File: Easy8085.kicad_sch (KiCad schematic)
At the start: 37 parts, among them J1 5V Power, J2 EXPANSION, J3 FTDI, SW1 RESET, U1 8085, U2 74LS139, U3 74LS573, U4 CY62256, U5 X28256, U6 8251A, U7 74LS90, Y1 6.144M

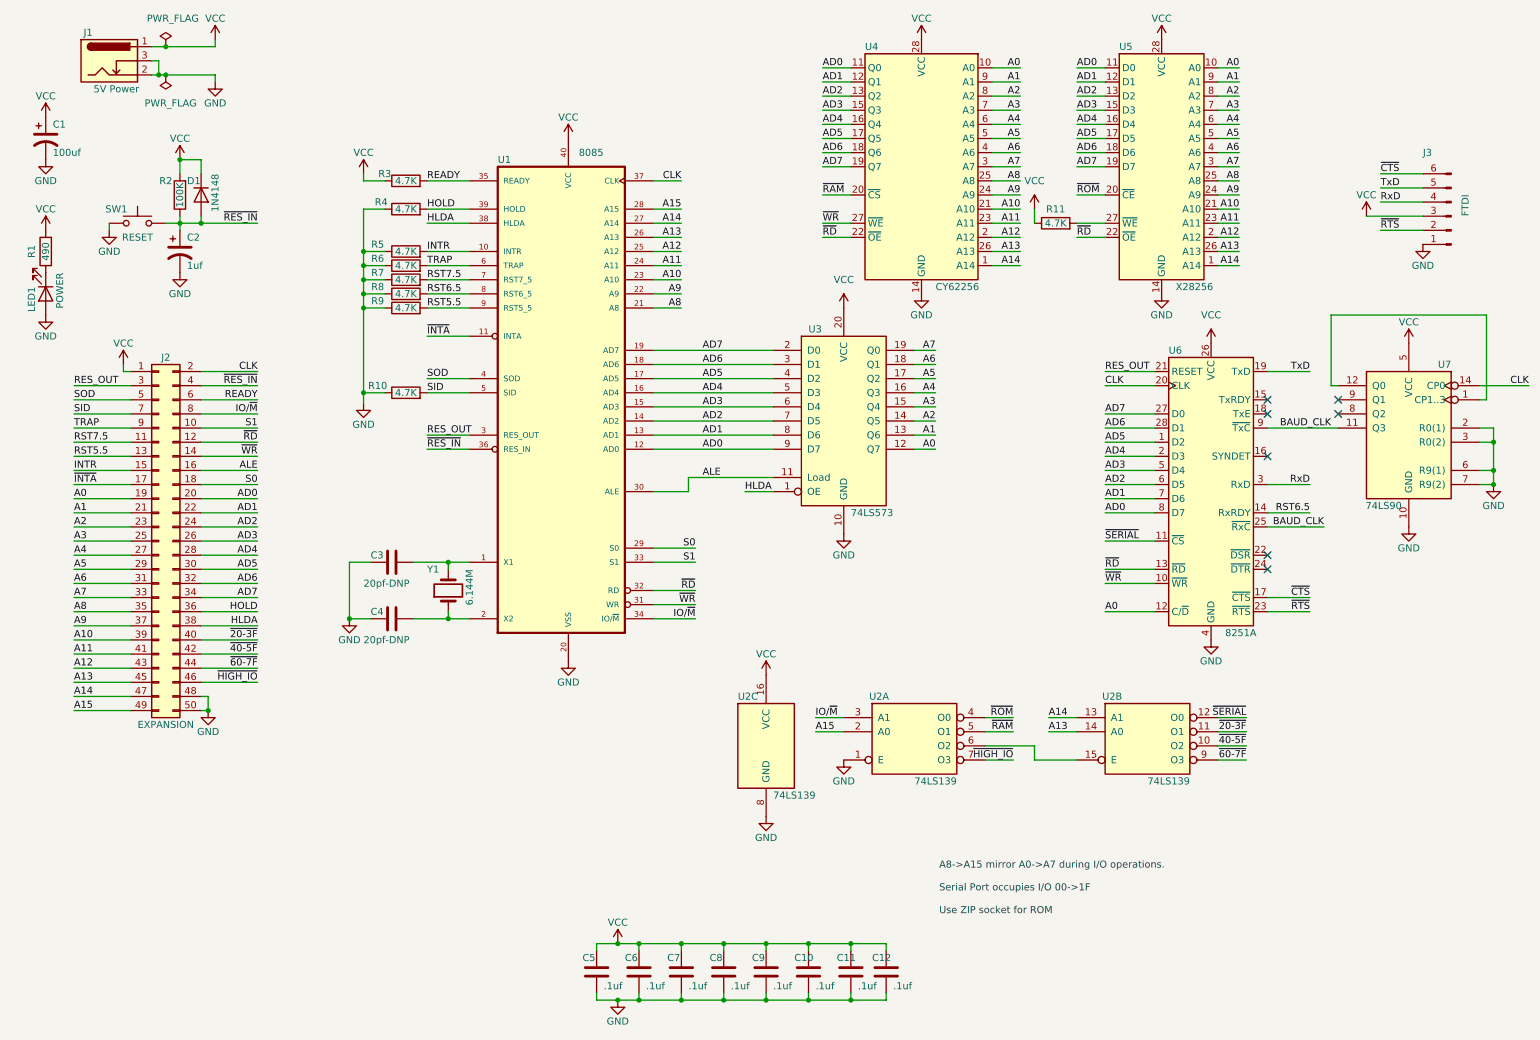
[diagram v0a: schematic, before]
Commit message: re-working PCB and schematic to seperate expansion connector and reduce parts.
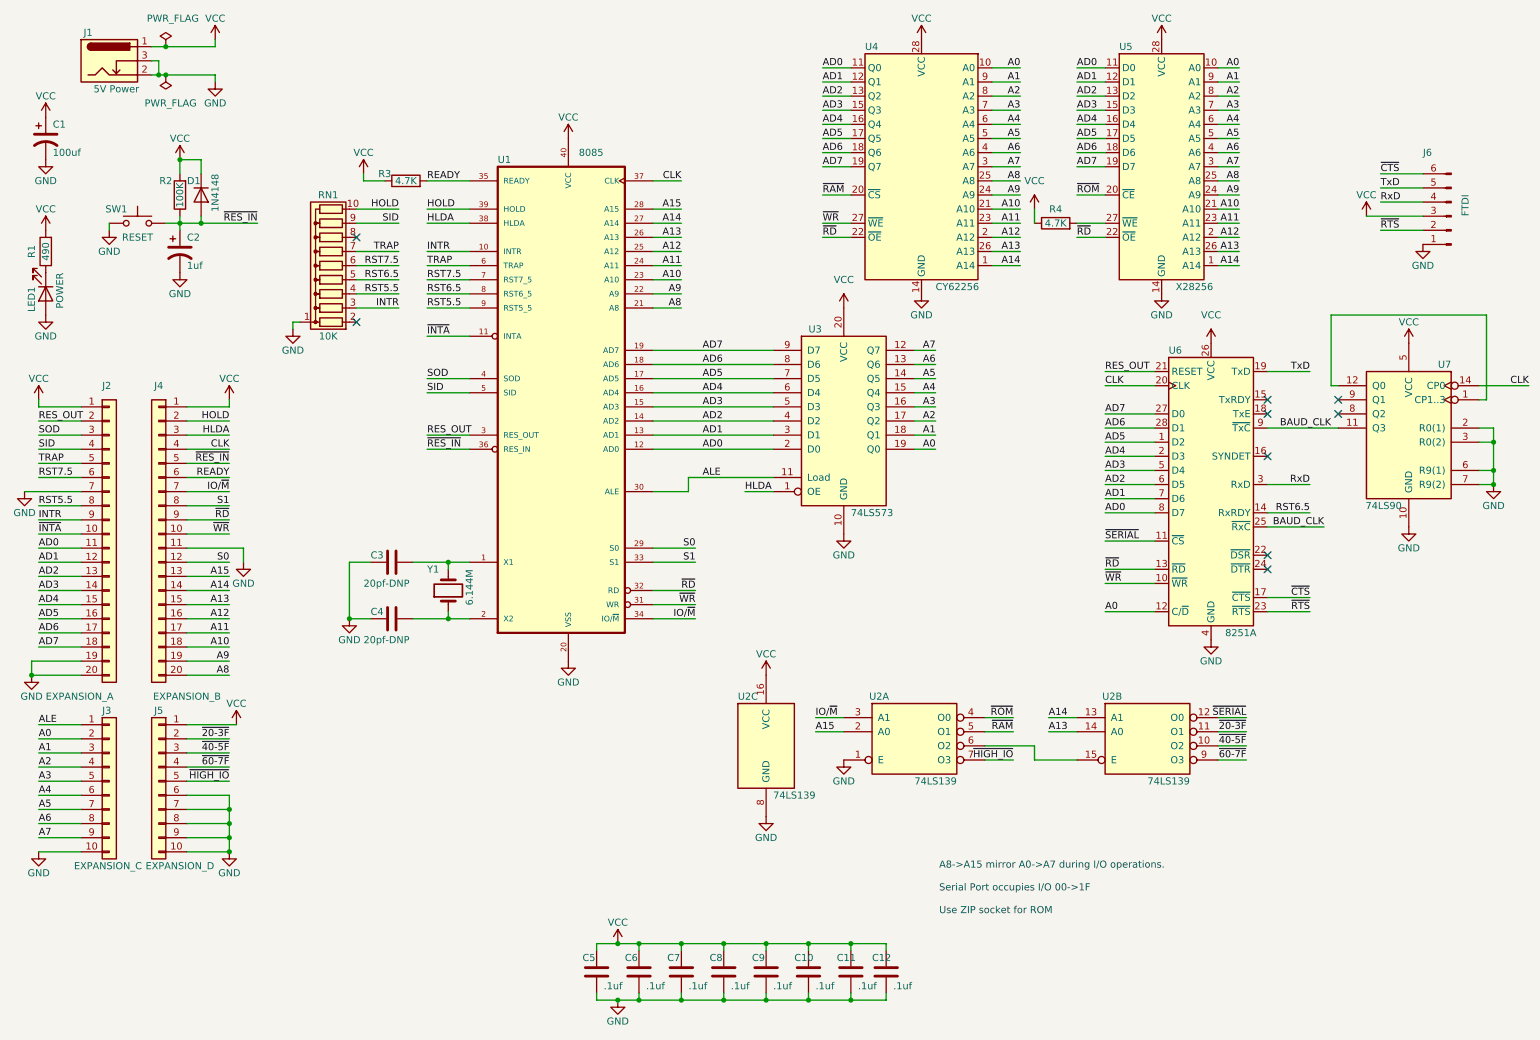
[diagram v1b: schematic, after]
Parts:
- removed J2: EXPANSION, Connector_PinHeader_2.54mm:PinHeader_2x25_P2.54mm_Vertical, symbol Connector_Generic:Conn_02x25_Odd_Even
- removed R10, R4, R5, R6, R7, R8, R9: 4.7K, Resistor_THT:R_Axial_DIN0204_L3.6mm_D1.6mm_P7.62mm_Horizontal, symbol Device:R
- added J2: EXPANSION_A, Connector_PinHeader_2.54mm:PinHeader_1x20_P2.54mm_Vertical, symbol Connector_Generic:Conn_01x20
- added J3: EXPANSION_C, Connector_PinHeader_2.54mm:PinHeader_1x10_P2.54mm_Vertical, symbol Connector_Generic:Conn_01x10
- added J4: EXPANSION_B, Connector_PinHeader_2.54mm:PinHeader_1x20_P2.54mm_Vertical, symbol Connector_Generic:Conn_01x20
- added J5: EXPANSION_D, Connector_PinHeader_2.54mm:PinHeader_1x10_P2.54mm_Vertical, symbol Connector_Generic:Conn_01x10
- added RN1: 10K, Resistor_THT:R_Array_SIP10, symbol Device:R_Network09
- U1: footprint Package_DIP:DIP-40_W15.24mm -> Package_DIP:DIP-40_W15.24mm_Socket
- U2: footprint Package_DIP:DIP-16_W7.62mm -> Package_DIP:DIP-16_W7.62mm_Socket
- U3: footprint Package_DIP:DIP-20_W7.62mm -> Package_DIP:DIP-20_W7.62mm_Socket
- U4, U6: footprint Package_DIP:DIP-28_W15.24mm -> Package_DIP:DIP-28_W15.24mm_Socket
- U7: footprint Package_DIP:DIP-14_W7.62mm -> Package_DIP:DIP-14_W7.62mm_Socket
- renumbered J3 to J6, R11 to R4
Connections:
- net A0: now also U3.19 (Q0), J3.2 (Pin_2); no longer U3.12 (Q7)
- net A1: now also U3.18 (Q1), J3.3 (Pin_3); no longer U3.13 (Q6)
- net A10: now also J4.18 (Pin_18)
- net A11: now also J4.17 (Pin_17)
- net A12: now also J4.16 (Pin_16)
- net A13: now also J4.15 (Pin_15)
- net A14: now also J4.14 (Pin_14)
- net A15: now also J4.13 (Pin_13)
- net A2: now also U3.17 (Q2), J3.4 (Pin_4); no longer U3.14 (Q5)
- net A3: now also U3.16 (Q3), J3.5 (Pin_5); no longer U3.15 (Q4)
- net A4: now also U3.15 (Q4), J3.6 (Pin_6); no longer U3.16 (Q3)
- net A5: now also U3.14 (Q5), J3.7 (Pin_7); no longer U3.17 (Q2)
- net A6: now also U3.13 (Q6), J3.8 (Pin_8); no longer U3.18 (Q1)
- net A7: now also U3.12 (Q7), J3.9 (Pin_9); no longer U3.19 (Q0)
- net A8: now also J4.20 (Pin_20)
- net A9: now also J4.19 (Pin_19)
- net AD0: now also U3.2 (D0), J2.11 (Pin_11); no longer U3.9 (D7)
- net AD1: now also U3.3 (D1), J2.12 (Pin_12); no longer U3.8 (D6)
- net AD2: now also U3.4 (D2), J2.13 (Pin_13); no longer U3.7 (D5)
- net AD3: now also U3.5 (D3), J2.14 (Pin_14); no longer U3.6 (D4)
- net AD4: now also U3.6 (D4), J2.15 (Pin_15); no longer U3.5 (D3)
- net AD5: now also U3.7 (D5), J2.16 (Pin_16); no longer U3.4 (D2)
- net AD6: now also U3.8 (D6), J2.17 (Pin_17); no longer U3.3 (D1)
- net AD7: now also U3.9 (D7), J2.18 (Pin_18); no longer U3.2 (D0)
- net ALE: now also J3.1 (Pin_1)
- net CLK: now also J4.4 (Pin_4)
- net GND: now also J2.19 (Pin_19), J2.20 (Pin_20), J2.7 (Pin_7), J3.10 (Pin_10), J4.11 (Pin_11), J5.10 (Pin_10), J5.6 (Pin_6), J5.7 (Pin_7), J5.8 (Pin_8), J5.9 (Pin_9), RN1.1 (common)
- net HLDA: now also J4.3 (Pin_3)
- net HOLD: now also J4.2 (Pin_2), RN1.10 (R9)
- net INTR: now also J2.9 (Pin_9), RN1.3 (R2)
- net IO/~{M}: now also J4.7 (Pin_7)
- net READY: now also J4.6 (Pin_6)
- net RES_OUT: now also J2.2 (Pin_2)
- net RST5.5: now also J2.8 (Pin_8), RN1.4 (R3)
- net RST6.5: now also RN1.5 (R4)
- net RST7.5: now also J2.6 (Pin_6), RN1.6 (R5)
- net S0: now also J4.12 (Pin_12)
- net S1: now also J4.8 (Pin_8)
- net SID: now also J2.4 (Pin_4), RN1.9 (R8)
- net SOD: now also J2.3 (Pin_3)
- net TRAP: now also J2.5 (Pin_5), RN1.7 (R6)
- net VCC: now also J2.1 (Pin_1), J4.1 (Pin_1), J5.1 (Pin_1)
- net ~{20-3F}: now also J5.2 (Pin_2)
- net ~{40-5F}: now also J5.3 (Pin_3)
- net ~{60-7F}: now also J5.4 (Pin_4)
- net ~{HIGH_IO}: now also J5.5 (Pin_5)
- net ~{INTA}: now also J2.10 (Pin_10)
- net ~{RD}: now also J4.9 (Pin_9)
- net ~{RES_IN}: now also J4.5 (Pin_5)
- net ~{WR}: now also J4.10 (Pin_10)
- no-connect marks 7 -> 9

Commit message: Continuing PCB layout.
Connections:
- net ALE: now also J3.10 (Pin_10); no longer J3.1 (Pin_1)
- net GND: now also J3.1 (Pin_1); no longer J3.10 (Pin_10)
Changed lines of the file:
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@@
     (stroke (width 0) (type default) (color 0 0 0 0))
   )
-  (wire (pts (xy 16.51 142.24) (xy 24.13 142.24))
+  (wire (pts (xy 13.97 142.24) (xy 24.13 142.24))
     (stroke (width 0) (type default) (color 0 0 0 0))
   )
@@
     (effects (font (size 1.27 1.27)) (justify right bottom))
   )
-  (label "ALE" (at 16.51 142.24 0)
+  (label "ALE" (at 16.51 165.1 0)
     (effects (font (size 1.27 1.27)) (justify left bottom))
   )
@@
     (effects (font (size 1.27 1.27)) (justify left bottom))
   )
-  (symbol (lib_id "power:GND") (at 16.51 165.1 0) (unit 1)
+  (symbol (lib_id "power:GND") (at 13.97 142.24 0) (unit 1)
     (in_bom yes) (on_board yes)
-    (property "Reference" "#PWR04" (id 0) (at 16.51 171.45 0)
+    (property "Reference" "#PWR04" (id 0) (at 13.97 148.59 0)
       (effects (font (size 1.27 1.27)) hide)
     )
-    (property "Value" "GND" (id 1) (at 16.51 168.91 0))
-    (property "Footprint" "" (id 2) (at 16.51 165.1 0)
+    (property "Value" "GND" (id 1) (at 13.97 146.05 0))
+    (property "Footprint" "" (id 2) (at 13.97 142.24 0)
       (effects (font (size 1.27 1.27)) hide)
     )
-    (property "Datasheet" "" (id 3) (at 16.51 165.1 0)
+    (property "Datasheet" "" (id 3) (at 13.97 142.24 0)
       (effects (font (size 1.27 1.27)) hide)
     )

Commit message: 4 layer board continued...
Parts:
- removed J2: EXPANSION_A, Connector_PinHeader_2.54mm:PinHeader_1x20_P2.54mm_Vertical, symbol Connector_Generic:Conn_01x20
- removed J3: EXPANSION_C, Connector_PinHeader_2.54mm:PinHeader_1x10_P2.54mm_Vertical, symbol Connector_Generic:Conn_01x10
- removed J4: EXPANSION_B, Connector_PinHeader_2.54mm:PinHeader_1x20_P2.54mm_Vertical, symbol Connector_Generic:Conn_01x20
- removed J5: EXPANSION_D, Connector_PinHeader_2.54mm:PinHeader_1x10_P2.54mm_Vertical, symbol Connector_Generic:Conn_01x10
- added J2: Expansion, Connector_PinHeader_2.54mm:PinHeader_2x25_P2.54mm_Vertical, symbol Connector_Generic:Conn_02x25_Odd_Even
- renumbered J6 to J3
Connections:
- net A0: now also U3.12 (Q7), J2.20 (Pin_20); no longer U3.19 (Q0)
- net A1: now also U3.13 (Q6), J2.24 (Pin_24); no longer U3.18 (Q1)
- net A10: now also J2.27 (Pin_27)
- net A11: now also J2.25 (Pin_25)
- net A12: now also J2.23 (Pin_23)
- net A13: now also J2.21 (Pin_21)
- net A14: now also J2.19 (Pin_19)
- net A15: now also J2.17 (Pin_17)
- net A2: now also U3.14 (Q5), J2.28 (Pin_28); no longer U3.17 (Q2)
- net A3: now also U3.15 (Q4), J2.32 (Pin_32); no longer U3.16 (Q3)
- net A4: now also U3.16 (Q3), J2.36 (Pin_36); no longer U3.15 (Q4)
- net A5: now also U3.17 (Q2), J2.40 (Pin_40); no longer U3.14 (Q5)
- net A6: now also U3.18 (Q1), J2.44 (Pin_44); no longer U3.13 (Q6)
- net A7: now also U3.19 (Q0), J2.48 (Pin_48); no longer U3.12 (Q7)
- net A8: now also J2.31 (Pin_31)
- net A9: now also J2.29 (Pin_29)
- net AD0: now also U3.9 (D7), J2.18 (Pin_18); no longer U3.2 (D0)
- net AD1: now also U3.8 (D6), J2.22 (Pin_22); no longer U3.3 (D1)
- net AD2: now also U3.7 (D5), J2.26 (Pin_26); no longer U3.4 (D2)
- net AD3: now also U3.6 (D4), J2.30 (Pin_30); no longer U3.5 (D3)
- net AD4: now also U3.5 (D3), J2.34 (Pin_34); no longer U3.6 (D4)
- net AD5: now also U3.4 (D2), J2.38 (Pin_38); no longer U3.7 (D5)
- net AD6: now also U3.3 (D1), J2.42 (Pin_42); no longer U3.8 (D6)
- net AD7: now also U3.2 (D0), J2.46 (Pin_46); no longer U3.9 (D7)
- net CLK: now also J2.7 (Pin_7)
- net GND: now also J2.37 (Pin_37), J2.39 (Pin_39), J2.49 (Pin_49), J2.50 (Pin_50)
- net HLDA: now also J2.5 (Pin_5)
- net HOLD: now also J2.3 (Pin_3)
- net INTR: now also J2.14 (Pin_14)
- net IO/~{M}: now also J2.11 (Pin_11)
- net RES_OUT: now also J2.2 (Pin_2)
- net RST5.5: now also J2.12 (Pin_12)
- net RST7.5: now also J2.10 (Pin_10)
- net SID: now also J2.6 (Pin_6)
- net SOD: now also J2.4 (Pin_4)
- net TRAP: now also J2.8 (Pin_8)
- net VCC: now also J2.1 (Pin_1), J2.33 (Pin_33), J2.35 (Pin_35)
- net ~{20-3F}: now also J2.41 (Pin_41)
- net ~{40-5F}: now also J2.43 (Pin_43)
- net ~{60-7F}: now also J2.45 (Pin_45)
- net ~{HIGH_IO}: now also J2.47 (Pin_47)
- net ~{INTA}: now also J2.16 (Pin_16)
- net ~{RD}: now also J2.13 (Pin_13)
- net ~{RES_IN}: now also J2.9 (Pin_9)
- net ~{WR}: now also J2.15 (Pin_15)

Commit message: Finally making progress on the layout.
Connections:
- net S0: no longer names the net of U1.29 (S0)
- net S1: no longer names the net of U1.33 (S1)
- no-connect marks 9 -> 11
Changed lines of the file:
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@@
   (no_connect (at 237.49 111.76))
   (no_connect (at 237.49 114.3))
+  (no_connect (at 127 110.49))
+  (no_connect (at 127 113.03))
   (wire (pts (xy 203.2 39.37) (xy 208.28 39.37))
     (stroke (width 0) (type default) (color 0 0 0 0))
@@
     (stroke (width 0) (type default) (color 0 0 0 0))
   )
-  (wire (pts (xy 127 110.49) (xy 134.62 110.49))
-    (stroke (width 0) (type default) (color 0 0 0 0))
-  )
   (wire (pts (xy 63.5 69.85) (xy 62.23 69.85))
     (stroke (width 0) (type default) (color 0 0 0 0))
@@
   )
   (wire (pts (xy 38.1 25.4) (xy 39.37 25.4))
-    (stroke (width 0) (type default) (color 0 0 0 0))
-  )
-  (wire (pts (xy 127 113.03) (xy 134.62 113.03))
     (stroke (width 0) (type default) (color 0 0 0 0))
   )
@@
     (effects (font (size 1.27 1.27)) (justify left bottom))
   )
-  (label "S0" (at 134.62 110.49 180)
-    (effects (font (size 1.27 1.27)) (justify right bottom))
-  )
   (label "RST5.5" (at 19.05 97.79 0)
     (effects (font (size 1.27 1.27)) (justify left bottom))
@@
     (effects (font (size 1.27 1.27)) (justify left bottom))
   )
-  (label "S1" (at 134.62 113.03 180)
-    (effects (font (size 1.27 1.27)) (justify right bottom))
-  )
   (label "A13" (at 46.99 110.49 180)

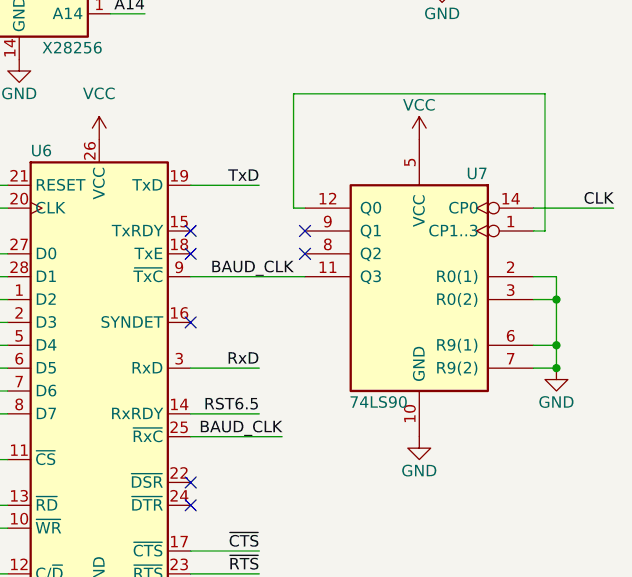
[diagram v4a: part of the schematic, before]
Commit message: Finished board routing.  Need to fix silkscreen
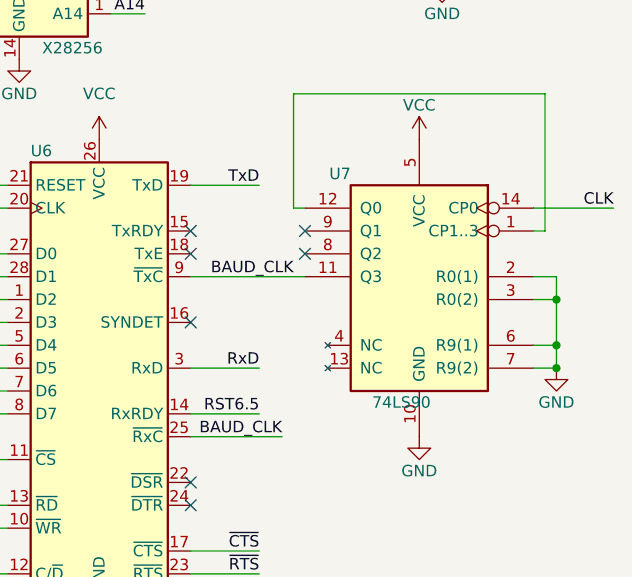
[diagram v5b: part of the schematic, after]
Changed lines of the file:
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@@
   (symbol (lib_id "74xx:74LS90") (at 262.89 88.9 0) (mirror y) (unit 1)
     (in_bom yes) (on_board yes)
-    (property "Reference" "U7" (id 0) (at 270.51 77.47 0)
+    (property "Reference" "U7" (id 0) (at 255.27 77.47 0)
       (effects (font (size 1.27 1.27)) (justify left))
     )
-    (property "Value" "74LS90" (id 1) (at 261.62 102.87 0)
+    (property "Value" "74LS90" (id 1) (at 264.16 102.87 0)
       (effects (font (size 1.27 1.27)) (justify left))
     )
-    (property "Footprint" "Package_DIP:DIP-14_W7.62mm_Socket" (id 2) (at 262.89 88.9 0)
+    (property "Footprint" "Package_DIP:DIP-14_W7.62mm_Socket" (id 2) (at 227.33 72.39 0)
       (effects (font (size 1.27 1.27)) hide)
     )
-    (property "Datasheet" "http://www.ti.com/lit/gpn/sn74LS90" (id 3) (at 262.89 88.9 0)
+    (property "Datasheet" "http://www.ti.com/lit/gpn/sn74LS90" (id 3) (at 229.87 101.6 0)
       (effects (font (size 1.27 1.27)) hide)
     )
+    (pin "13")
+    (pin "4")
     (pin "1")
     (pin "10")
